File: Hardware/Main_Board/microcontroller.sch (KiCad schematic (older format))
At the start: 71 parts, among them K1 CONN_3, K11 CONN_3, K2 CONN_3, K3 CONN_3, K4 CONN_3, K5 CONN_3, K6 CONN_3, K7 CONN_3, K8 CONN_3, P10 CONN_4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

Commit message: [HARDWARE][MAIN_BOARD] Fix some mistakes
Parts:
- added K12: CONN_3, symbol CONN_3
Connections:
- net AX12_POWER: now also K11.2 (PM); no longer K11.1 (P1)
- net DAC1: now also P6.2 (P2); no longer P6.1 (P1)
- net DAC2: now also P6.3 (P3); no longer P6.2 (P2)
- net GND: now also P6.1 (P1), K12.2 (PM), K12.3 (P3); no longer P6.3 (P3)
- net UART_AX12_RX: now also K11.1 (P1); no longer K11.2 (PM)
- net VDD: now also K12.1 (P1)

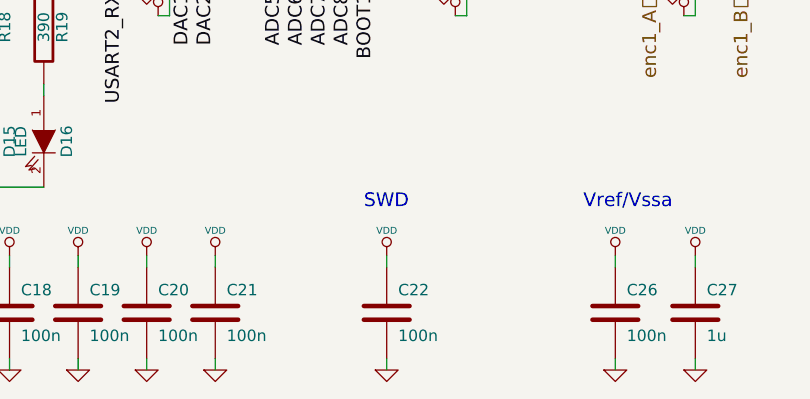
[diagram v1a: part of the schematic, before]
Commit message: [HARDWARE][MAIN_BOARD]Add the forgotten capacitance
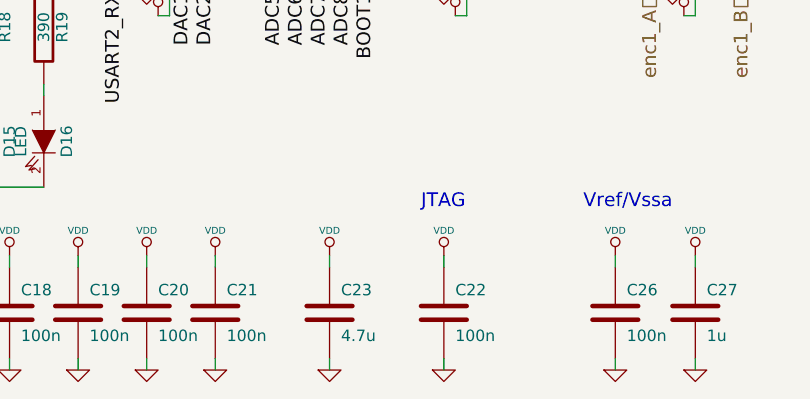
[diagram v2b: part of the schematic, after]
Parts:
- added C23: 4.7u, symbol C
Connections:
- net GND: now also C23.2
- net VDD: now also C23.1
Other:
- note added: "JTAG"
- note removed: "SWD"
- moved on the sheet: C22

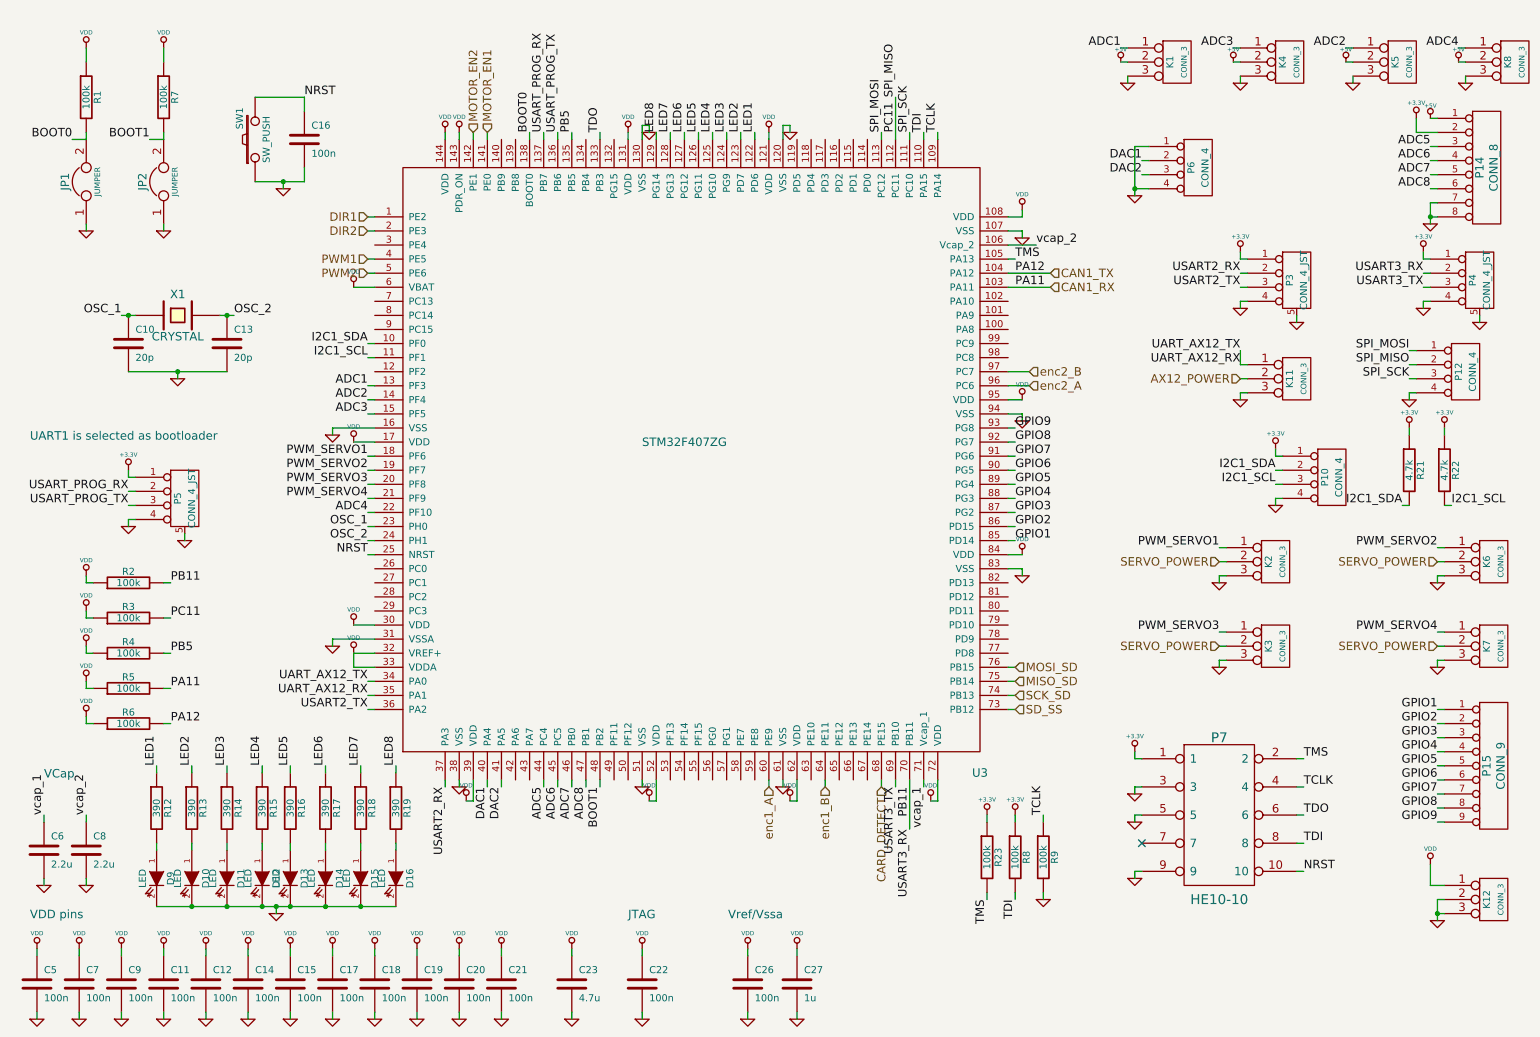
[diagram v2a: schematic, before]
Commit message: [HARDWARE] add pulldown on L298 enable pins, change boot select circuitry, add pullup on USART1, add serigraphy
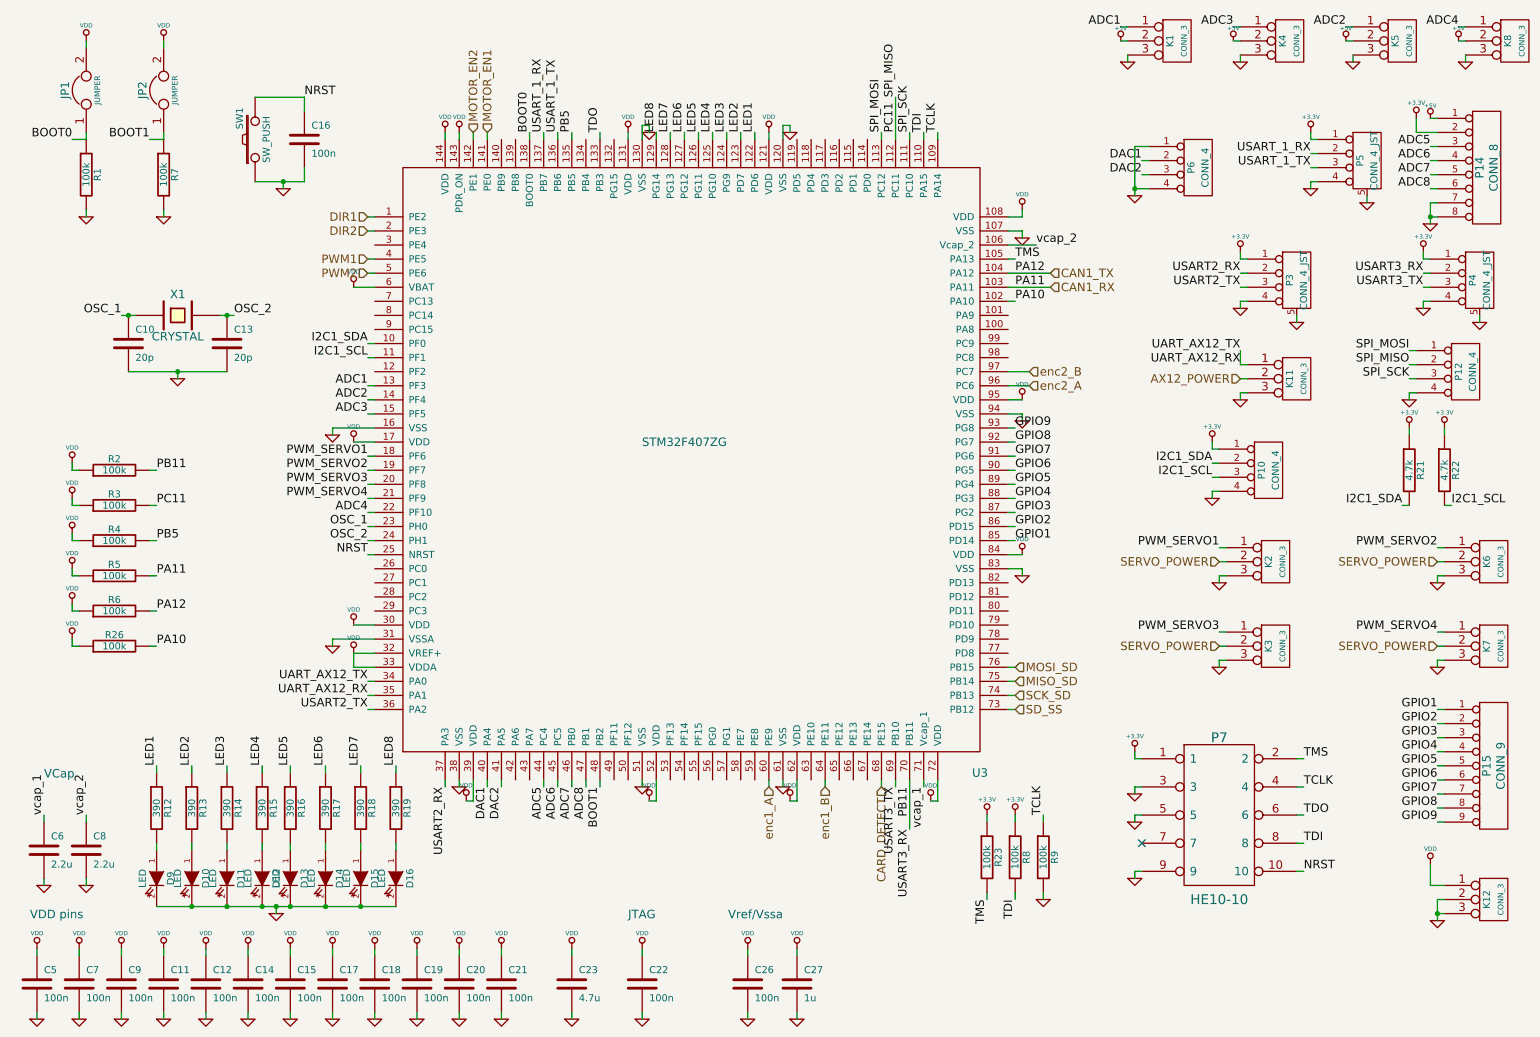
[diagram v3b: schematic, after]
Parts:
- added R26: 100k, symbol R
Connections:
- net BOOT0: now also JP1.1, R1.1; no longer JP1.2, R1.2
- net BOOT1: now also JP2.1, R7.1; no longer JP2.2, R7.2
- net GND: now also R1.2, R7.2; no longer JP1.1, JP2.1
- net VDD: now also JP1.2, JP2.2, R26.1; no longer R1.1, R7.1
- net PA10: now reaches U3.102 (PA10)
- net PA10: now also R26.2
- net USART_PROG_RX renamed USART_1_RX
- net USART_PROG_TX renamed USART_1_TX
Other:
- note removed: "UART1 is selected as bootloader"
- moved on the sheet: JP1, JP2, K1, K4, K5, K8, P10, P5, R1, R2, R3, R4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
